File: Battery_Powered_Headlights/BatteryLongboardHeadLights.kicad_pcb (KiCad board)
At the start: 2 copper layers, 76.2 x 10.8 mm, 16 parts, among them P1 CONN_01X03, U1 AL8805

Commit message: PCB work in progress
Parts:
- removed D4: D_Schottky, Light_Parts:PowerDI-123
- removed JP1: JUMPER3, Connect:GS3
- removed P1: CONN_01X03, Connectors_Molex:Molex_KK-6410-03_03x2.54mm_Straight
- added BT1: Battery_Cell, Battery_Holders:Keystone_1042_1x18650, F.Cu at (145.9, 93.2)
- added J1: USB_OTG, Connectors:USB_Micro-B, F.Cu at (99.7, 87.0)
- added Q1: DMN2040LTS-13, Housings_SSOP:TSSOP-8_4.4x3mm_Pitch0.65mm, B.Cu at (116.7, 94.7)
- added R4: 20K, Resistors_SMD:R_0603, B.Cu at (122.9, 91.4)
- added R5: 1K, Resistors_SMD:R_0603, B.Cu at (122.9, 89.9)
- added R6: 0.3, Resistors_SMD:R_0805, B.Cu at (177.0, 90.0)
- added SW1: SW_Push, Light_Parts:GPTS203212B, F.Cu at (98.7, 97.8)
- added U2: MCP73833T, Housings_DFN_QFN:DFN-10-1EP_3x3mm_Pitch0.5mm, B.Cu at (122.8, 87.2)
- added U3: AP5724, Housings_DFN_QFN:DFN-6-1EP_2x2mm_Pitch0.65mm, B.Cu at (175.9, 92.8)
- C1: value 4.7uF -> 0.1uF; footprint Capacitors_SMD:C_0805 -> Capacitors_SMD:C_0603; moved to B.Cu
- C2: value 2.2uF -> 4.7uF; footprint Capacitors_SMD:C_0603 -> Capacitors_SMD:C_0805; moved to B.Cu
- C3: value 1uF -> 4.7uF; footprint Capacitors_SMD:C_0603_HandSoldering -> Capacitors_SMD:C_0603; moved to B.Cu
- C4: value 1uF -> 10uF; footprint Capacitors_SMD:C_0603_HandSoldering -> Capacitors_SMD:C_0603; moved to B.Cu
- C5: value 1uF -> 4.7uF; footprint Capacitors_SMD:C_0603_HandSoldering -> Capacitors_SMD:C_0805; moved to B.Cu
- D1: value LED -> D_Schottky; footprint LEDs:LED-XP-G_CREE -> Diodes_SMD:D_SOD-123F; moved to B.Cu
- D2, D3: footprint LEDs:LED-XP-G_CREE -> LEDs:LED_Cree-XP-G
- L1: value INDUCTOR -> 22uH; footprint Light_Parts:Inductor5x5 -> Inductors_SMD:L_Taiyo-Yuden_NR-40xx; moved to B.Cu
- R1: value 0.3 -> 2.2K; moved to B.Cu
- R2: value 38000 -> 330; moved to B.Cu
- R3: value 10000 -> 10K; moved to B.Cu
- U1: value AL8805 -> bq29700; footprint TO_SOT_Packages_SMD:SOT-23-5 -> Housings_SON:WSON6_1.5x1.5mm_Pitch0.5mm; moved to B.Cu
- moved C5 77.7 mm to (118.9, 87.2), turned to 90 degrees
- moved R1 38.0 mm to (115.6, 91.4)
- moved C1 38.0 mm to (117.1, 91.4), turned to 270 degrees
- moved U1 36.5 mm to (113.8, 91.3), turned to 90 degrees
- moved R3 33.4 mm to (104.4, 98.2), turned to 0 degrees
- moved C2 27.7 mm to (127.0, 87.2), turned to 90 degrees
- moved L1 26.3 mm to (170.5, 94.2), turned to 270 degrees
- moved R2 18.6 mm to (118.6, 91.4), turned to 90 degrees
- moved D2 15.0 mm to (192.4, 100.1)
- moved D1 12.0 mm to (175.1, 95.5)
- moved C3 10.5 mm to (173.5, 91.9), turned to 90 degrees
- moved D3 6.69 mm to (192.4, 86.2), turned to 0 degrees
- moved C4 5.31 mm to (179.6, 93.0), turned to 90 degrees
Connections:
- C1 pad 1: VCC -> Net-(C1-Pad1)
- C1 pad 2: GND -> /VBAT_NEG
- C2 pad 1: VCC -> +BATT
- C3 pad 1: Net-(C3-Pad1) -> +BATT
- C3 pad 2: Net-(C3-Pad2) -> GND
- C4 pad 1: Net-(C3-Pad2) -> Net-(C4-Pad1)
- C4 pad 2: Net-(C4-Pad2) -> GND
- C5 pad 1: Net-(C4-Pad2) -> /USB_IN
- C5 pad 2: Net-(C5-Pad2) -> GND
- D1 pad 1: Net-(C3-Pad2) -> Net-(C4-Pad1)
- D1 pad 2: Net-(C3-Pad1) -> Net-(D1-Pad2)
- D2 pad 1: Net-(C4-Pad2) -> Net-(D2-Pad1)
- D2 pad 2: Net-(C3-Pad2) -> Net-(C4-Pad1)
- D2 pad 3: GND -> (no net)
- D3 pad 1: Net-(C5-Pad2) -> Net-(D3-Pad1)
- D3 pad 2: Net-(C4-Pad2) -> Net-(D2-Pad1)
- D3 pad 3: GND -> (no net)
- L1 pad 1: Net-(C5-Pad2) -> +BATT
- L1 pad 2: Net-(D4-Pad2) -> Net-(D1-Pad2)
- R1 pad 1: VCC -> Net-(R1-Pad1)
- R1 pad 2: Net-(C3-Pad1) -> /VBAT_NEG
- R2 pad 1: VCC -> +BATT
- R2 pad 2: Net-(JP1-Pad1) -> Net-(C1-Pad1)
- R3 pad 1: Net-(JP1-Pad1) -> /SWITCH
- U1 pad 1: Net-(D4-Pad2) -> Net-(U1-Pad1)
- U1 pad 2: GND -> Net-(Q1-Pad5)
- U1 pad 3: /CTRL -> Net-(Q1-Pad4)
- U1 pad 4: Net-(C3-Pad1) -> /VBAT_NEG
- U1 pad 5: VCC -> Net-(C1-Pad1)
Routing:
- net +BATT: track 0.00 -> 108.2 mm, vias 0 -> 2
- net /SWITCH: track 0.00 -> 89.2 mm, vias 0 -> 2
- net Net-(C5-Pad2): track 69.8 -> 0.00 mm, vias 6 -> 0
- net GND: track 61.6 -> 0.00 mm, vias 31 -> 0
- net VCC: track 37.6 -> 0.00 mm
- net Net-(C4-Pad2): track 22.2 -> 0.00 mm
- net Net-(C3-Pad2): track 22.0 -> 0.00 mm
- net /USB_IN: track 0.00 -> 18.9 mm, vias 0 -> 1
- net Net-(C3-Pad1): track 17.1 -> 0.00 mm
- net /CTRL: track 14.4 -> 0.00 mm
- net Net-(R4-Pad1): track 0.00 -> 7.06 mm, vias 0 -> 2
- net Net-(Q1-Pad5): track 0.00 -> 7.02 mm
- net Net-(C1-Pad1): track 0.00 -> 6.46 mm
- net Net-(C4-Pad1): track 0.00 -> 6.28 mm, vias 0 -> 2
- net Net-(R5-Pad1): track 0.00 -> 5.99 mm, vias 0 -> 2
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- removed copper zone on B.Cu, net GND
- removed copper zone on F.Cu, net GND
- removed copper zone on F.Cu, net Net-(C5-Pad2)
- removed copper zone on F.Cu, net VCC
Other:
- board outline removed
- net class Default: clearance 0.2 -> 0
- rule trace_clearance: 0.2 -> 0
- rule trace_min: 0.2 -> 0.13
- board text removed: "GiS ENGINEERING MG"
- board text removed: "REVISION 1 2/17"
- board text removed: "WARNING: BRIGHT!"

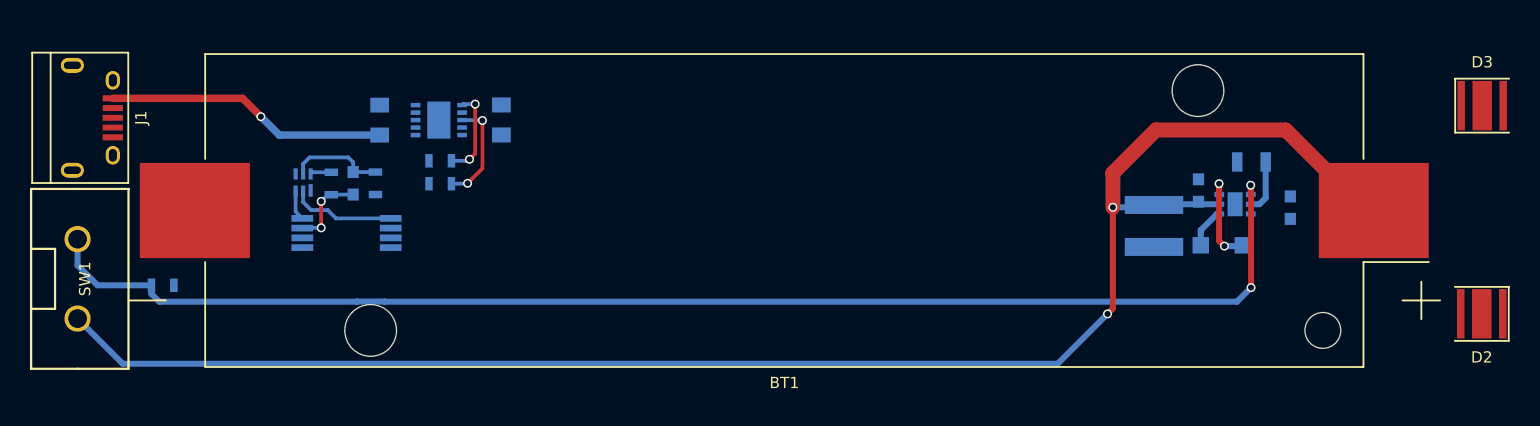
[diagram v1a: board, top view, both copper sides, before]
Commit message: PCB layout for the Batteryboard/LEDcontroller done
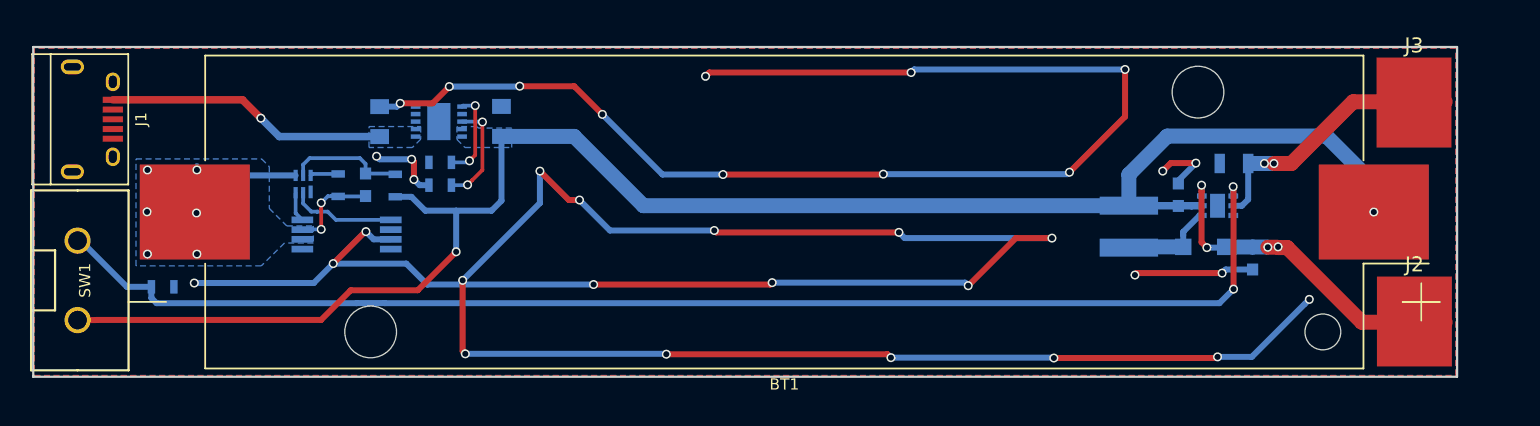
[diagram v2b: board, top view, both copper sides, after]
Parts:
- removed D2, D3: LED, LEDs:LED_Cree-XP-G
- added J2: Conn_01x01, Global_Parts:SolderWirePad_single_SMD_5x6mm, F.Cu at (187.9, 100.6)
- added J3: Conn_01x01, Global_Parts:SolderWirePad_single_SMD_5x6mm, F.Cu at (187.9, 86.0)
- moved C4 4.21 mm to (177.1, 96.4), turned to 270 degrees
- moved L1 1.68 mm to (168.9, 94.3)
- moved C3 1.37 mm to (172.2, 92.1)
- moved R2 1.33 mm to (119.9, 91.5)
- moved D1 1.17 mm to (173.9, 95.6)
- moved R6 1.17 mm to (175.9, 90.1)
- moved U3 1.17 mm to (174.8, 92.9)
- moved C1 0.83 mm to (117.9, 91.5)
- moved R1 0.47 mm to (116.1, 91.5)
- moved BT1 0.10 mm to (145.9, 93.3)
- moved C5 0.10 mm to (118.9, 87.3)
- moved J1 0.10 mm to (99.7, 87.1)
- moved R3 0.10 mm to (104.4, 98.3)
- moved R4 0.10 mm to (122.9, 91.5)
- moved U1 0.10 mm to (113.8, 91.4)
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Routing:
- net GND: track 0.00 -> 276.1 mm, vias 0 -> 35
- net /VBAT_NEG: track 5.36 -> 33.4 mm, vias 2 -> 8
- net Net-(C4-Pad1): track 6.28 -> 23.1 mm, vias 2 -> 4
- net Net-(D3-Pad1): track 3.57 -> 18.2 mm, vias 0 -> 2
- net +BATT: track 108.2 -> 114.6 mm
- net Net-(D1-Pad2): track 2.69 -> 6.35 mm
- net /SWITCH: track 89.2 -> 87.2 mm
- net Net-(C1-Pad1): track 6.46 -> 7.87 mm
- net Net-(R1-Pad1): track 1.43 -> 2.04 mm
- added copper zone on B.Cu, net +BATT
- added copper zone on B.Cu, net /USB_IN
- added copper zone on B.Cu, net /VBAT_NEG
- added copper zone on B.Cu, net GND
- added copper zone on F.Cu, net GND
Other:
- board outline added: 95 x 22 mm

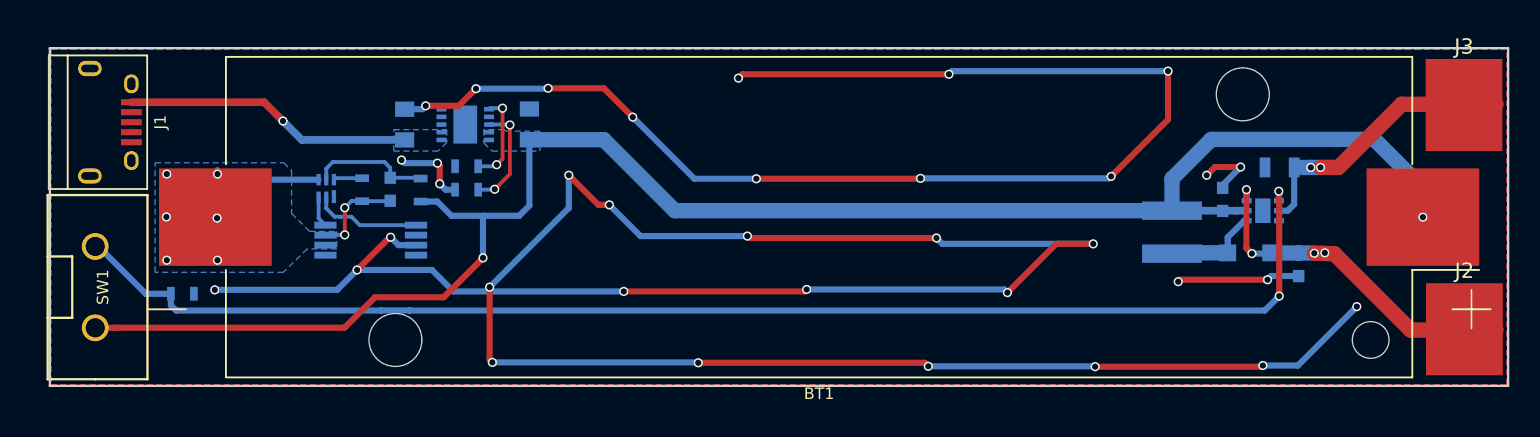
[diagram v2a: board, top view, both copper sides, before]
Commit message: PCB's should now be orderable
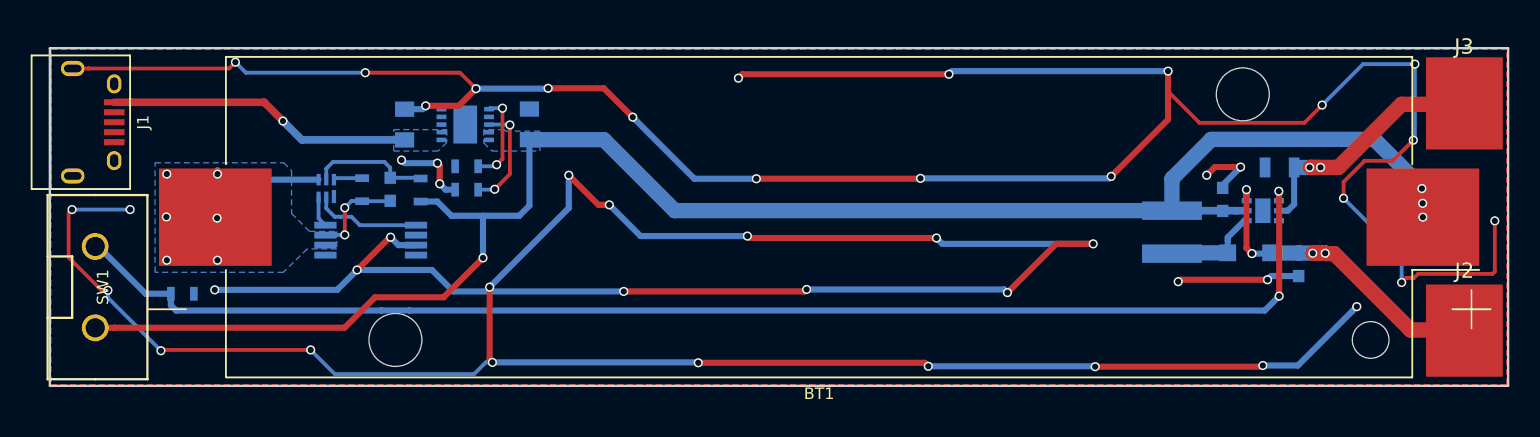
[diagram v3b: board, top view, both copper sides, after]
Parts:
- moved J1 1.12 mm to (98.6, 87.1)
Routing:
- net GND: track 276.1 -> 389.9 mm, vias 35 -> 48
- net /USB_IN: track 18.9 -> 20.0 mm
- net +BATT: vias 2 -> 4

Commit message: updating designs for newest revision; removing unneeded files
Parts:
- removed J2, J3: Conn_01x01, Global_Parts:SolderWirePad_single_SMD_5x6mm
- added D2: LED, LEDs:LED_Cree-XP-G, F.Cu at (150.7, 105.3)
- added D3: LED, LEDs:LED_Cree-XP-G, F.Cu at (161.2, 105.3)
- C1, C2, C3, C4, C5, D1, L1, R1, R2, R3, R4, R5, R6, U1, U2, U3: moved to F.Cu
- Q1: value DMN2040LTS-13 -> DMN2028UFDH-7; footprint Housings_SSOP:TSSOP-8_4.4x3mm_Pitch0.65mm -> Housings_DFN_QFN:DFN-8-1EP_3x3mm_Pitch0.65mm; moved to F.Cu
- moved SW1 68.2 mm to (148.5, 51.3), turned to 0 degrees
- moved J1 54.3 mm to (137.1, 48.8), turned to 0 degrees
- moved U1 51.5 mm to (159.6, 114.8)
- moved R3 47.5 mm to (151.8, 96.1), turned to 90 degrees
- moved Q1 47.4 mm to (161.2, 111.0), turned to 90 degrees
- moved R1 47.2 mm to (157.1, 115.0)
- moved C1 44.5 mm to (155.6, 115.2)
- moved C5 42.5 mm to (151.7, 114.3), turned to 0 degrees
- moved R2 42.0 mm to (156.5, 112.0), turned to 270 degrees
- moved R4 38.1 mm to (154.9, 112.1), turned to 270 degrees
- moved R5 37.7 mm to (153.5, 112.1), turned to 270 degrees
- moved U2 36.8 mm to (150.8, 111.2), turned to 90 degrees
- moved R6 27.2 mm to (150.0, 98.3), turned to 90 degrees
- moved C2 26.3 mm to (146.3, 105.2), turned to 180 degrees
- moved BT1 23.5 mm to (157.0, 72.7), turned to 0 degrees
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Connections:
- Q1 pad 1: Net-(Q1-Pad1) -> GND
- Q1 pad 2: /VBAT_NEG -> Net-(Q1-Pad2)
- Q1 pad 6: GND -> Net-(Q1-Pad6)
- Q1 pad 7: GND -> Net-(Q1-Pad7)
- U1 pad 2: Net-(Q1-Pad5) -> Net-(Q1-Pad2)
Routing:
- net GND: track 389.9 -> 0.00 mm, vias 48 -> 0
- net +BATT: track 114.6 -> 8.42 mm, vias 4 -> 0
- net /SWITCH: track 87.2 -> 1.24 mm, vias 2 -> 0
- net /VBAT_NEG: track 33.4 -> 0.00 mm, vias 8 -> 0
- net Net-(C4-Pad1): track 23.2 -> 0.00 mm, vias 4 -> 0
- net /USB_IN: track 20.0 -> 0.00 mm, vias 1 -> 0
- net Net-(D3-Pad1): track 17.7 -> 2.22 mm, vias 2 -> 0
- net Net-(Q1-Pad5): track 7.02 -> 0.00 mm
- net Net-(D1-Pad2): track 6.35 -> 0.00 mm
- net Net-(Q1-Pad2): track 0.00 -> 5.44 mm, vias 0 -> 2
- net Net-(R5-Pad1): track 5.99 -> 3.10 mm, vias 2 -> 0
- net Net-(C1-Pad1): track 7.87 -> 5.89 mm
- net Net-(Q1-Pad4): track 2.50 -> 3.86 mm
- net Net-(R4-Pad1): track 7.06 -> 6.17 mm, vias 2 -> 0
- removed copper zone on B.Cu, net +BATT
- removed copper zone on B.Cu, net /USB_IN
- removed copper zone on B.Cu, net /VBAT_NEG
- removed copper zone on B.Cu, net GND
- removed copper zone on F.Cu, net GND
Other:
- board size 95 x 22 mm -> 24 x 24 mm
- net class Default: clearance 0 -> 0.13
- rule trace_clearance: 0 -> 0.13
